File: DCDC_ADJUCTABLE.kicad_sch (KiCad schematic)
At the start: 43 parts, among them Q301 BSS138L, Q302 NVTFWS4D9N04XMTAG, Q303 NVTFWS4D9N04XMTAG, U301 TPS62933, U302 TPS62933, U303 LM74700, U304 LM74700

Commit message: progress on CORE pcb
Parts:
- C1009: renamed from C311; now left out of the parts list
- C1020: renamed from C312; now left out of the parts list
- renumbered C301 to C1001, C303 to C1002, C305 to C1003, C309 to C1004, C313 to C1005, C317 to C1006, C323 to C1007, C307 to C1008, C315 to C1010, C319 to C1011, C321 to C1012, C302 to C1013, C304 to C1014, C306 to C1015, C310 to C1016, C314 to C1017, C318 to C1018, C324 to C1019, C316 to C1021, C320 to C1022, C322 to C1023, C308 to C1024, L301 to L1001, L302 to L1002, Q302 to Q1001, Q303 to Q1002, Q301 to Q1003, R306 to R1001, R304 to R1002, R307 to R1003, R301 to R1004, R302 to R1005, R308 to R1006, R309 to R1007, R1102 to R1008, R303 to R1009, R305 to R1010, U301 to U1001, U303 to U1002, U302 to U1003, U304 to U1004

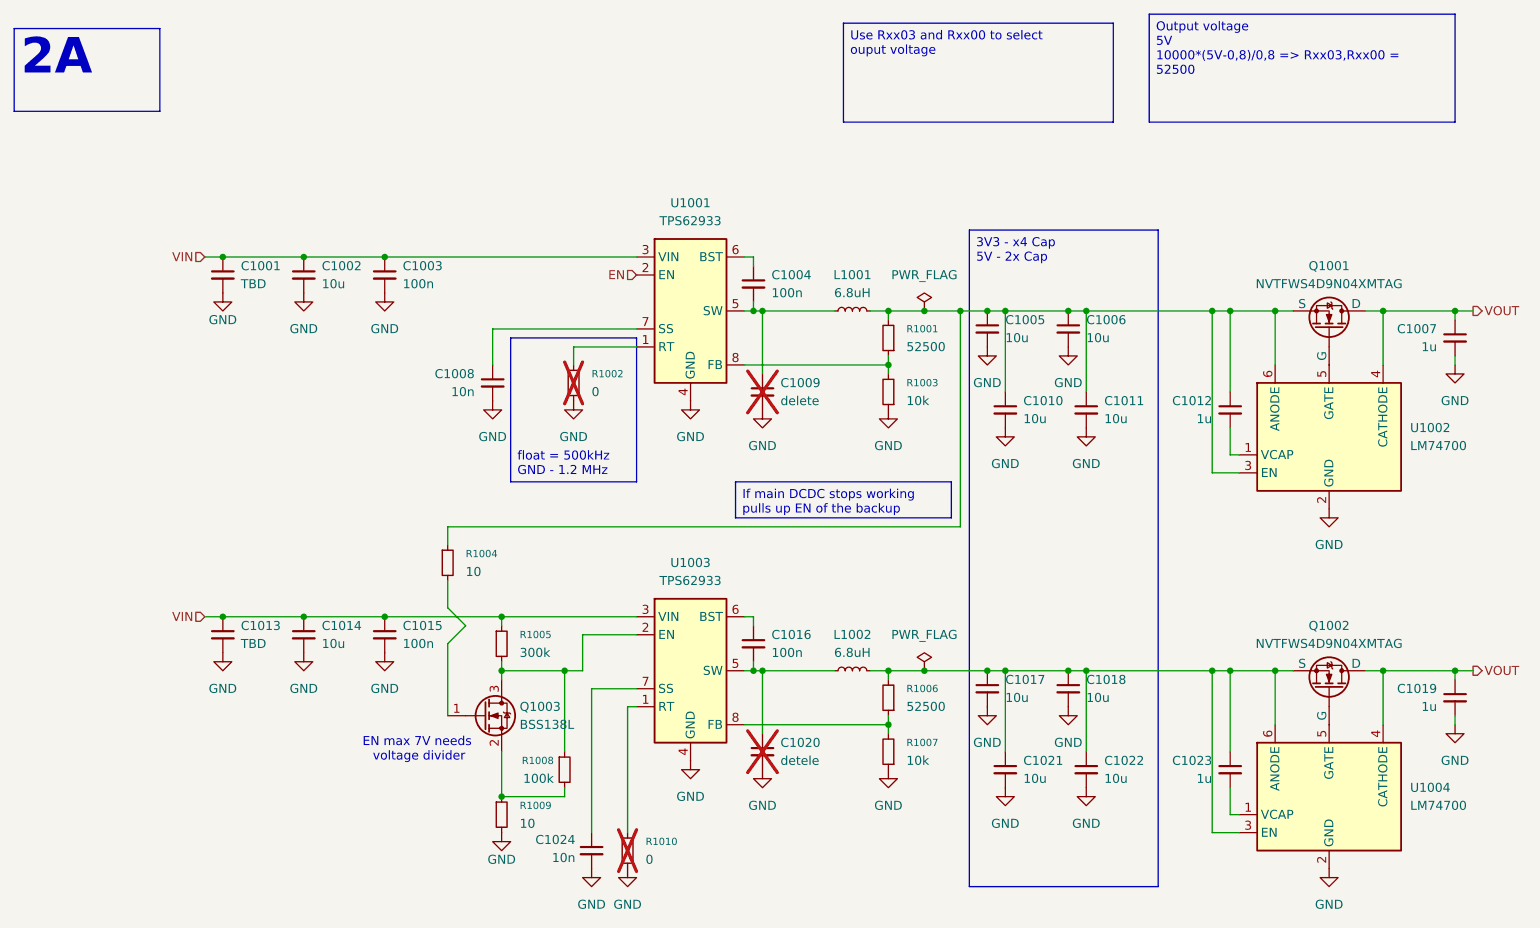
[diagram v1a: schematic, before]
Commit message: pcb progres for all components
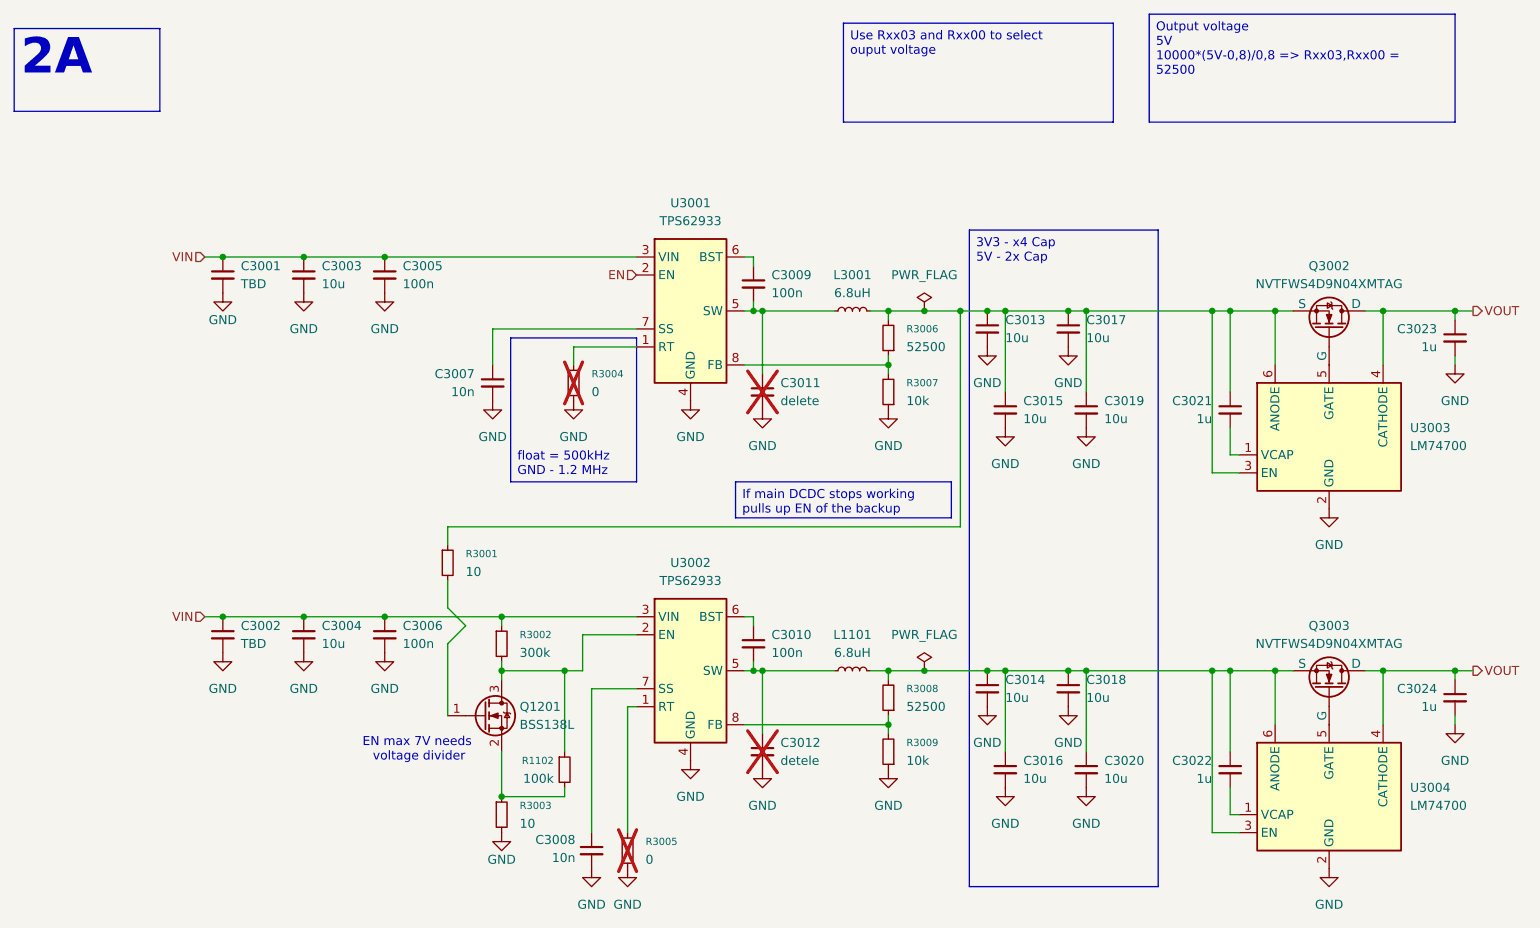
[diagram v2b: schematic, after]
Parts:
- renumbered C1001 to C3001, C1013 to C3002, C1002 to C3003, C1014 to C3004, C1003 to C3005, C1015 to C3006, C1008 to C3007, C1024 to C3008, C1004 to C3009, C1016 to C3010, C1009 to C3011, C1020 to C3012, C1005 to C3013, C1017 to C3014, C1010 to C3015, C1021 to C3016, C1006 to C3017, C1018 to C3018, C1011 to C3019, C1022 to C3020, C1012 to C3021, C1023 to C3022, C1007 to C3023, C1019 to C3024, L1002 to L1101, L1001 to L3001, Q1003 to Q1201, Q1001 to Q3002, Q1002 to Q3003, R1008 to R1102, R1004 to R3001, R1005 to R3002, R1009 to R3003, R1002 to R3004, R1010 to R3005, R1001 to R3006, R1003 to R3007, R1006 to R3008, R1007 to R3009, U1001 to U3001, U1003 to U3002, U1002 to U3003, U1004 to U3004

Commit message: progress on PCBs
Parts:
- renumbered C3001 to C201, C3003 to C202, C3005 to C203, C3009 to C204, C3013 to C205, C3017 to C206, C3023 to C207, C3007 to C208, C3011 to C209, C3015 to C210, C3019 to C211, C3021 to C212, C3002 to C213, C3004 to C214, C3006 to C215, C3010 to C216, C3014 to C217, C3018 to C218, C3024 to C219, C3012 to C220, C3016 to C221, C3020 to C222, C3022 to C223, C3008 to C224, L3001 to L201, L1101 to L202, Q3002 to Q201, Q3003 to Q202, Q1201 to Q203, R3006 to R201, R3004 to R202, R3007 to R203, R3001 to R204, R3002 to R205, R3008 to R206, R3009 to R207, R1102 to R208, R3003 to R209, R3005 to R210, U3001 to U201, U3003 to U202, U3002 to U203, U3004 to U204
